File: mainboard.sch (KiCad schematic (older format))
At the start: 32 parts, among them J1 105017-1001, J2 Conn_01x04_Female, J3 Conn_01x02_Female, J4 Conn_01x09_Female, J5 Conn_01x02_Female, J6 Conn_01x02_Female, J7 Conn_01x04_Female, Q1 AOD4184A, U1 ESP32-WROOM-32E_(16MB), U3 AMS1117-3.3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

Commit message: MAND
elco
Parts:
- removed C3: 22u, Capacitor_SMD:C_0805_2012Metric_Pad1.18x1.45mm_HandSolder, symbol Device:C
- removed C8: 470u, Capacitor_SMD:C_0805_2012Metric_Pad1.18x1.45mm_HandSolder, symbol Device:C
- added C3: 470u, Capacitor_SMD:CP_Elec_6.3x5.4, symbol Device:CP
- added C8: 22u, Capacitor_SMD:CP_Elec_6.3x5.4, symbol Device:CP
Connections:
- net 3V3: now also C8.1
- net 5V: now also C3.1
- net GND: now also C3.2, C8.2
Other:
- note added: "Hoofdmodule ESP32\n\n"
- note removed: "Hoofdmodule ESP32\n="
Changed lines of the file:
@@
-$EndComp
-$Comp
-L Device:C C8
-U 1 1 60524F4F
-P 4950 6450
-F 0 "C8" H 5065 6496 50  0000 L CNN
-F 1 "470u" H 5065 6405 50  0000 L CNN
-F 2 "Capacitor_SMD:C_0805_2012Metric_Pad1.18x1.45mm_HandSolder" H 4988 6300 50  0001 C CNN
-F 3 "~" H 4950 6450 50  0001 C CNN
-	1    4950 6450
-	1    0    0    -1
 $EndComp
 $Comp
@@
 SDA
 Text Notes 2250 1300 0    150  ~ 0
-Hoofdmodule ESP32\n=
+Hoofdmodule ESP32\n\n
 Text GLabel 3950 3150 2    50   Input ~ 0
 SDA
@@
 	0    -1   -1   0
 $EndComp
-$Comp
-L Device:C C3
-U 1 1 604CF650
-P 9750 1550
-F 0 "C3" H 9865 1596 50  0000 L CNN
-F 1 "22u" H 9865 1505 50  0000 L CNN
-F 2 "Capacitor_SMD:C_0805_2012Metric_Pad1.18x1.45mm_HandSolder" H 9788 1400 50  0001 C CNN
-F 3 "~" H 9750 1550 50  0001 C CNN
-	1    9750 1550
-	1    0    0    -1
-$EndComp
 Wire Wire Line
 	9350 1700 9750 1700
-Wire Wire Line
-	9650 1400 9750 1400
-Wire Wire Line
-	9750 1400 9950 1400
-Connection ~ 9750 1400
 Connection ~ 4900 1950
 Wire Wire Line
@@
 	0    -1   -1   0
 $EndComp
+$Comp
+L Device:CP C3
+U 1 1 604FA000
+P 4950 6450
+F 0 "C3" H 5068 6496 50  0000 L CNN
+F 1 "470u" H 5068 6405 50  0000 L CNN
+F 2 "Capacitor_SMD:CP_Elec_6.3x5.4" H 4988 6300 50  0001 C CNN
+F 3 "~" H 4950 6450 50  0001 C CNN
+	1    4950 6450
+	1    0    0    -1
+$EndComp
+$Comp
+L Device:CP C8
+U 1 1 604FE2E0
+P 9750 1550
+F 0 "C8" H 9868 1596 50  0000 L CNN
+F 1 "22u" H 9868 1505 50  0000 L CNN
+F 2 "Capacitor_SMD:CP_Elec_6.3x5.4" H 9788 1400 50  0001 C CNN
+F 3 "~" H 9750 1550 50  0001 C CNN
+	1    9750 1550
+	1    0    0    -1
+$EndComp
+Wire Wire Line
+	9650 1400 9750 1400
+Connection ~ 9750 1400
+Wire Wire Line
+	9750 1400 9950 1400
 $EndSCHEMATC

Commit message: wij waren de ir sensor vergeten, oeps
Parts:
- added J8: Conn_01x03_Female, Connector_PinSocket_2.54mm:PinSocket_1x03_P2.54mm_Vertical, symbol Connector:Conn_01x03_Female
- added SW1: SW_SPST, 434111043826:434111043826, symbol Switch:SW_SPST
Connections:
- wire segments 61 -> 59
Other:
- note added: "IR beam"
- moved on the sheet: J3
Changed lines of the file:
@@
 $EndComp
 Wire Wire Line
-	8200 1100 8450 1100
-Wire Wire Line
-	8450 1100 8450 1400
-Wire Wire Line
-	8450 1400 8800 1400
+	8600 1400 8800 1400
 Wire Wire Line
 	8200 1500 8450 1500
@@
 Text GLabel 8600 1100 2    50   Input ~ 0
 5V
-Wire Wire Line
-	8600 1100 8450 1100
-Connection ~ 8450 1100
 NoConn ~ 3900 6500
 NoConn ~ 3900 6600
@@
 INR
 NoConn ~ 2700 6600
-Text Notes 7765 5645 0    150  ~ 0
+Text Notes 7265 5745 0    150  ~ 0
 Pomp
 $Comp
 L Connector:Conn_01x02_Female J3
 U 1 1 6053B267
-P 7820 6160
-F 0 "J3" H 7712 5835 50  0000 C CNN
-F 1 "Conn_01x02_Female" H 7712 5926 50  0000 C CNN
-F 2 "Connector_PinSocket_2.54mm:PinSocket_1x02_P2.54mm_Vertical" H 7820 6160 50  0001 C CNN
-F 3 "~" H 7820 6160 50  0001 C CNN
-	1    7820 6160
-	-1   0    0    1
-$EndComp
-Text GLabel 8020 6060 2    50   Input ~ 0
+P 7320 6260
+F 0 "J3" H 7212 5935 50  0000 C CNN
+F 1 "Conn_01x02_Female" H 7212 6026 50  0000 C CNN
+F 2 "Connector_PinSocket_2.54mm:PinSocket_1x02_P2.54mm_Vertical" H 7320 6260 50  0001 C CNN
+F 3 "~" H 7320 6260 50  0001 C CNN
+	1    7320 6260
+	-1   0    0    1
+$EndComp
+Text GLabel 7520 6160 2    50   Input ~ 0
 Mosfet_Out-
-Text GLabel 8020 6160 2    50   Input ~ 0
+Text GLabel 7520 6260 2    50   Input ~ 0
 5V
 Text Notes 9775 4600 0    150  ~ 0
@@
 Wire Wire Line
 	9750 1400 9950 1400
+$Comp
+L Switch:SW_SPST SW1
+U 1 1 6050D5A1
+P 8400 1100
+F 0 "SW1" H 8400 1335 50  0000 C CNN
+F 1 "SW_SPST" H 8400 1244 50  0000 C CNN
+F 2 "434111043826:434111043826" H 8400 1100 50  0001 C CNN
+F 3 "~" H 8400 1100 50  0001 C CNN
+	1    8400 1100
+	1    0    0    -1
+$EndComp
+Wire Wire Line
+	8600 1100 8600 1400
+Text Notes 8115 5745 0    150  ~ 0
+IR beam
+$Comp
+L Connector:Conn_01x03_Female J8
+U 1 1 60521D0E
+P 8450 6225
+F 0 "J8" H 8342 5900 50  0000 C CNN
+F 1 "Conn_01x03_Female" H 8342 5991 50  0000 C CNN
+F 2 "Connector_PinSocket_2.54mm:PinSocket_1x03_P2.54mm_Vertical" H 8450 6225 50  0001 C CNN
+F 3 "~" H 8450 6225 50  0001 C CNN
+	1    8450 6225
+	-1   0    0    1
+$EndComp
+Text GLabel 8650 6125 2    50   Input ~ 0
+IRB
+Wire Notes Line
+	8072 5320 8072 6538
+Text GLabel 8650 6325 2    50   Input ~ 0
+3V3
+$Comp
+L power:GND #PWR?
+U 1 1 6055B549
+P 8650 6225
+F 0 "#PWR?" H 8650 5975 50  0001 C CNN
+F 1 "GND" V 8655 6097 50  0000 R CNN
+F 2 "" H 8650 6225 50  0001 C CNN
+F 3 "" H 8650 6225 50  0001 C CNN
+	1    8650 6225
+	0    -1   -1   0
+$EndComp
 $EndSCHEMATC

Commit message: lesupdate
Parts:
- removed SW1: SW_SPST, 434111043826:434111043826, symbol Switch:SW_SPST
- added S3: SWITCH-SPDT-SMD-RIGHT-ANGLE, SWITCH_SPST_SMD_A, symbol SparkFun-Switches:SWITCH-SPDT-SMD-RIGHT-ANGLE
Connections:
- net labels added: TFT_EN
- wire segments 59 -> 61
- no-connect marks 7 -> 8
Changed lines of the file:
@@
 Text GLabel 3950 3050 2    50   Input ~ 0
 TFT_MISO
-Text GLabel 3950 3550 2    50   Input ~ 0
-INR
 NoConn ~ 2700 6600
 Text Notes 7265 5745 0    150  ~ 0
@@
 Text GLabel 10400 6050 3    50   Input ~ 0
 TFT_MISO
-Text GLabel 10600 6050 3    50   Input ~ 0
-3V3
 Text GLabel 10500 6050 3    50   Input ~ 0
 TFT_CLK
@@
 Wire Wire Line
 	9750 1400 9950 1400
-$Comp
-L Switch:SW_SPST SW1
-U 1 1 6050D5A1
-P 8400 1100
-F 0 "SW1" H 8400 1335 50  0000 C CNN
-F 1 "SW_SPST" H 8400 1244 50  0000 C CNN
-F 2 "434111043826:434111043826" H 8400 1100 50  0001 C CNN
-F 3 "~" H 8400 1100 50  0001 C CNN
-	1    8400 1100
-	1    0    0    -1
-$EndComp
-Wire Wire Line
-	8600 1100 8600 1400
+Wire Wire Line
+	8600 1100 8600 1200
 Text Notes 8115 5745 0    150  ~ 0
 IR beam
@@
 3V3
 $Comp
-L power:GND #PWR?
+L power:GND #PWR0103
 U 1 1 6055B549
 P 8650 6225
-F 0 "#PWR?" H 8650 5975 50  0001 C CNN
+F 0 "#PWR0103" H 8650 5975 50  0001 C CNN
 F 1 "GND" V 8655 6097 50  0000 R CNN
 F 2 "" H 8650 6225 50  0001 C CNN
@@
 	0    -1   -1   0
 $EndComp
+$Comp
+L SparkFun-Switches:SWITCH-SPDT-SMD-RIGHT-ANGLE S3
+U 1 1 6053016E
+P 8300 1100
+F 0 "S3" H 8350 1476 45  0000 C CNN
+F 1 "SWITCH-SPDT-SMD-RIGHT-ANGLE" H 8350 1392 45  0000 C CNN
+F 2 "SWITCH_SPST_SMD_A" H 8300 1350 20  0001 C CNN
+F 3 "" H 8300 1100 50  0001 C CNN
+F 4 "SWCH-10651" H 8350 1297 60  0000 C CNN "Field4"
+	1    8300 1100
+	1    0    0    -1
+$EndComp
+Wire Wire Line
+	8500 1200 8600 1200
+Connection ~ 8600 1200
+Wire Wire Line
+	8600 1200 8600 1400
+NoConn ~ 8500 1000
+Text GLabel 3950 2850 2    50   Input ~ 0
+TFT_EN
+Text GLabel 10600 6050 3    50   Input ~ 0
+TFT_EN
+Text GLabel 3950 3550 2    50   Input ~ 0
+INR
 $EndSCHEMATC

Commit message: BIEPBOEP
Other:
- note removed: "Moet IO5 aan pullup?"
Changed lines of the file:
@@
 Wire Notes Line
 	470  5320 11210 5320
-Text Notes 5750 2250 0    50   ~ 0
-Moet IO5 aan pullup?
 Wire Notes Line
 	9170 2360 9170 6535

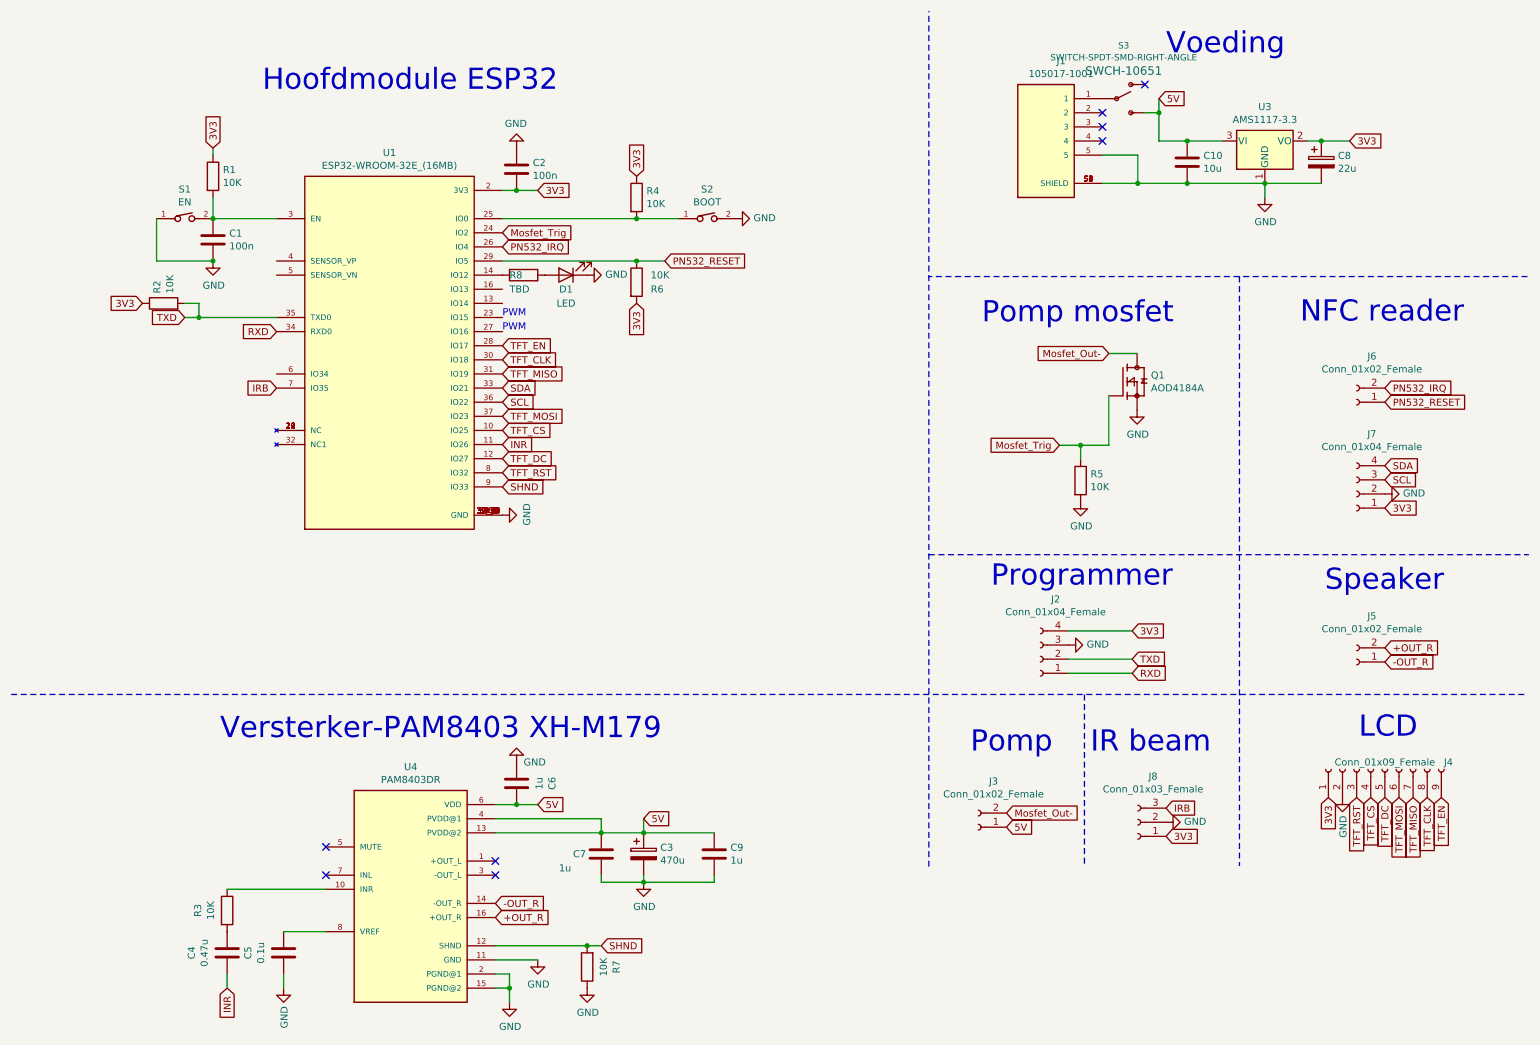
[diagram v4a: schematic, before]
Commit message: checken
update footprints caps
dubbele C8 verwijderd
nfc foute footprint opgelost
checken van alle esp en versterkerpinnen
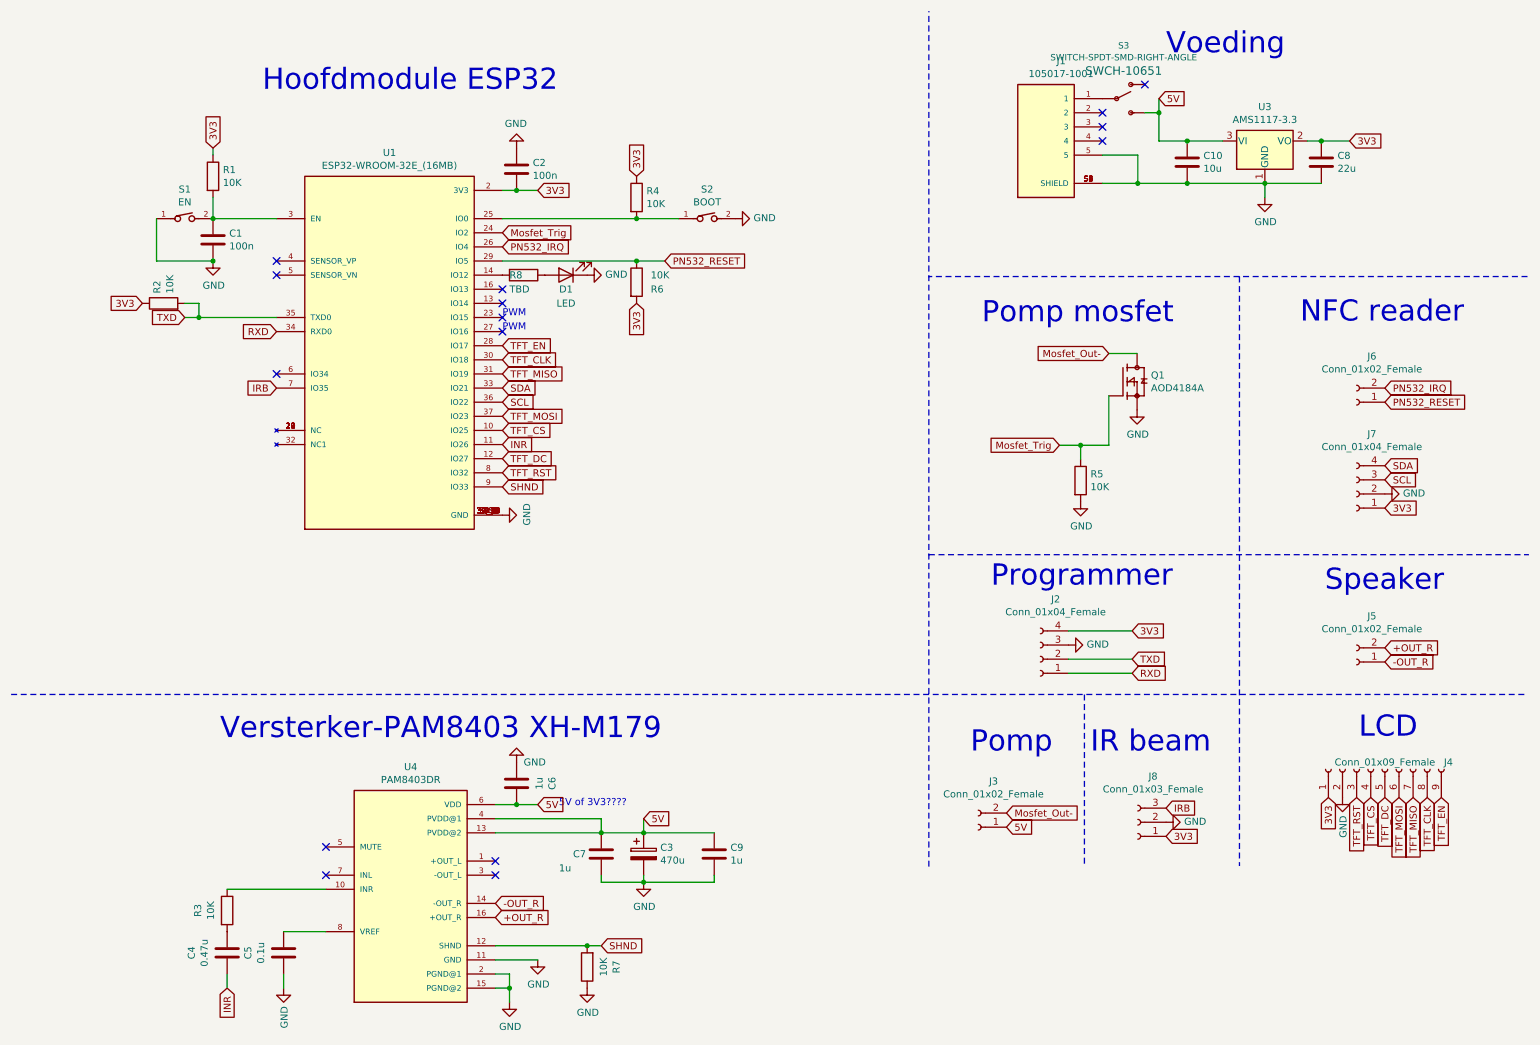
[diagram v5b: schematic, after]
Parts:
- removed C8: 22u, Capacitor_SMD:CP_Elec_6.3x5.4, symbol Device:CP
- added C8: 22u, mylibs:CAPPC3528X210N, symbol Device:C
- C3: footprint Capacitor_SMD:CP_Elec_6.3x5.4 -> Capacitor_THT:CP_Radial_D10.0mm_P5.00mm
- J7: footprint Connector_PinSocket_2.54mm:PinSocket_1x02_P2.54mm_Vertical -> Connector_PinSocket_2.54mm:PinSocket_1x04_P2.54mm_Vertical
- S3: footprint SWITCH_SPST_SMD_A -> Switches:SWITCH_SPST_SMD_A
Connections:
- net 3V3: now also C8.1
- net GND: now also C8.2
- no-connect marks 8 -> 15
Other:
- note added: "5V of 3V3????\n\n"
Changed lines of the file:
@@
 F 0 "J7" H 9892 3475 50  0000 C CNN
 F 1 "Conn_01x04_Female" H 9892 3566 50  0000 C CNN
-F 2 "Connector_PinSocket_2.54mm:PinSocket_1x02_P2.54mm_Vertical" H 10000 3900 50  0001 C CNN
+F 2 "Connector_PinSocket_2.54mm:PinSocket_1x04_P2.54mm_Vertical" H 10000 3900 50  0001 C CNN
 F 3 "~" H 10000 3900 50  0001 C CNN
 	1    10000 3900
@@
 F 0 "C3" H 5068 6496 50  0000 L CNN
 F 1 "470u" H 5068 6405 50  0000 L CNN
-F 2 "Capacitor_SMD:CP_Elec_6.3x5.4" H 4988 6300 50  0001 C CNN
+F 2 "Capacitor_THT:CP_Radial_D10.0mm_P5.00mm" H 4988 6300 50  0001 C CNN
 F 3 "~" H 4950 6450 50  0001 C CNN
 	1    4950 6450
 	1    0    0    -1
 $EndComp
-$Comp
-L Device:CP C8
-U 1 1 604FE2E0
-P 9750 1550
-F 0 "C8" H 9868 1596 50  0000 L CNN
-F 1 "22u" H 9868 1505 50  0000 L CNN
-F 2 "Capacitor_SMD:CP_Elec_6.3x5.4" H 9788 1400 50  0001 C CNN
-F 3 "~" H 9750 1550 50  0001 C CNN
-	1    9750 1550
-	1    0    0    -1
-$EndComp
-Wire Wire Line
-	9650 1400 9750 1400
-Connection ~ 9750 1400
-Wire Wire Line
-	9750 1400 9950 1400
 Wire Wire Line
 	8600 1100 8600 1200
@@
 F 0 "S3" H 8350 1476 45  0000 C CNN
 F 1 "SWITCH-SPDT-SMD-RIGHT-ANGLE" H 8350 1392 45  0000 C CNN
-F 2 "SWITCH_SPST_SMD_A" H 8300 1350 20  0001 C CNN
+F 2 "Switches:SWITCH_SPST_SMD_A" H 8300 1350 20  0001 C CNN
 F 3 "" H 8300 1100 50  0001 C CNN
 F 4 "SWCH-10651" H 8350 1297 60  0000 C CNN "Field4"
@@
 Text GLabel 3950 3550 2    50   Input ~ 0
 INR
+$Comp
+L Device:C C8
+U 1 1 605638F7
+P 9750 1550
+F 0 "C8" H 9865 1596 50  0000 L CNN
+F 1 "22u" H 9865 1505 50  0000 L CNN
+F 2 "mylibs:CAPPC3528X210N" H 9788 1400 50  0001 C CNN
+F 3 "~" H 9750 1550 50  0001 C CNN
+	1    9750 1550
+	1    0    0    -1
+$EndComp
+Wire Wire Line
+	9650 1400 9750 1400
+Connection ~ 9750 1400
+Wire Wire Line
+	9750 1400 9950 1400
+NoConn ~ 2350 3050
+NoConn ~ 2350 2350
+NoConn ~ 2350 2250
+NoConn ~ 3950 2550
+NoConn ~ 3950 2450
+NoConn ~ 3950 2650
+NoConn ~ 3950 2750
+Text Notes 4350 6200 0    50   ~ 0
+5V of 3V3????\n\n
 $EndSCHEMATC

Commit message: condensator vrij gemaakt en hoekjes gefixt
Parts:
- S3: symbol SparkFun-Switches:SWITCH-SPDT-SMD-RIGHT-ANGLE -> mainboard-rescue:SWITCH-SPDT-SMD-RIGHT-ANGLE-SparkFun-Switches
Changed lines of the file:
@@
 $EndComp
 $Comp
-L SparkFun-Switches:SWITCH-SPDT-SMD-RIGHT-ANGLE S3
+L mainboard-rescue:SWITCH-SPDT-SMD-RIGHT-ANGLE-SparkFun-Switches S3
 U 1 1 6053016E
 P 8300 1100

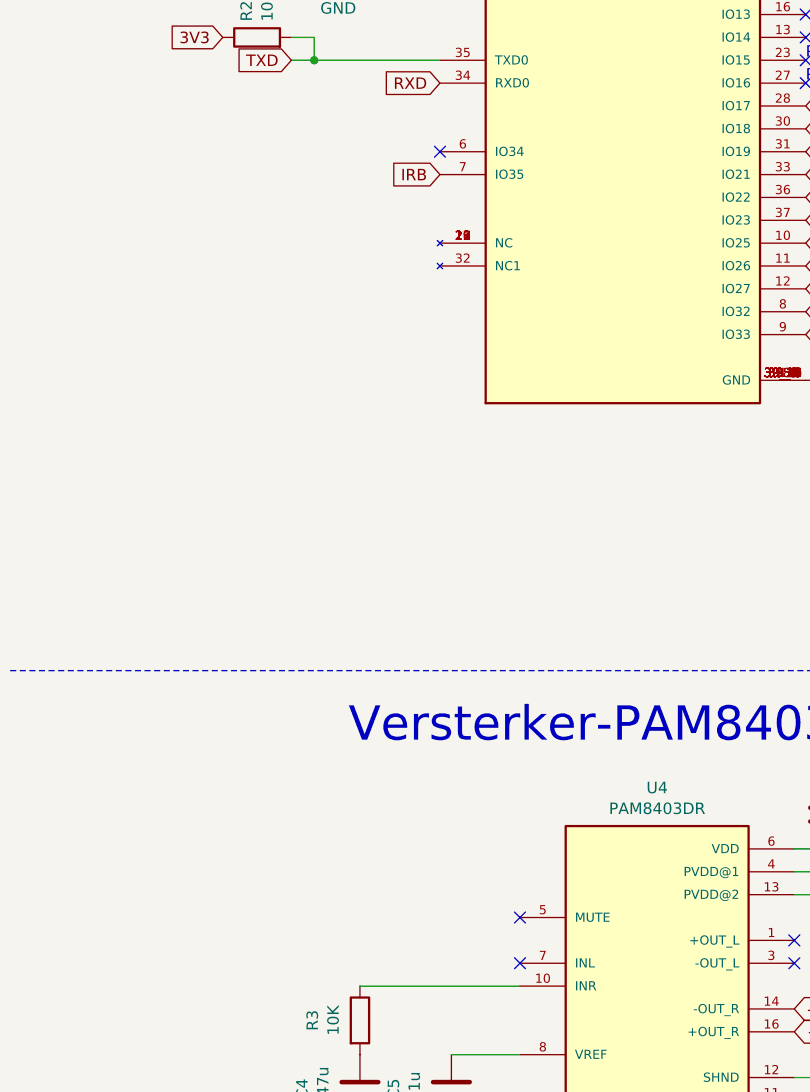
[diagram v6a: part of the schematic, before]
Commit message: fixes
-pullup aan IRB
-mute aan 5V
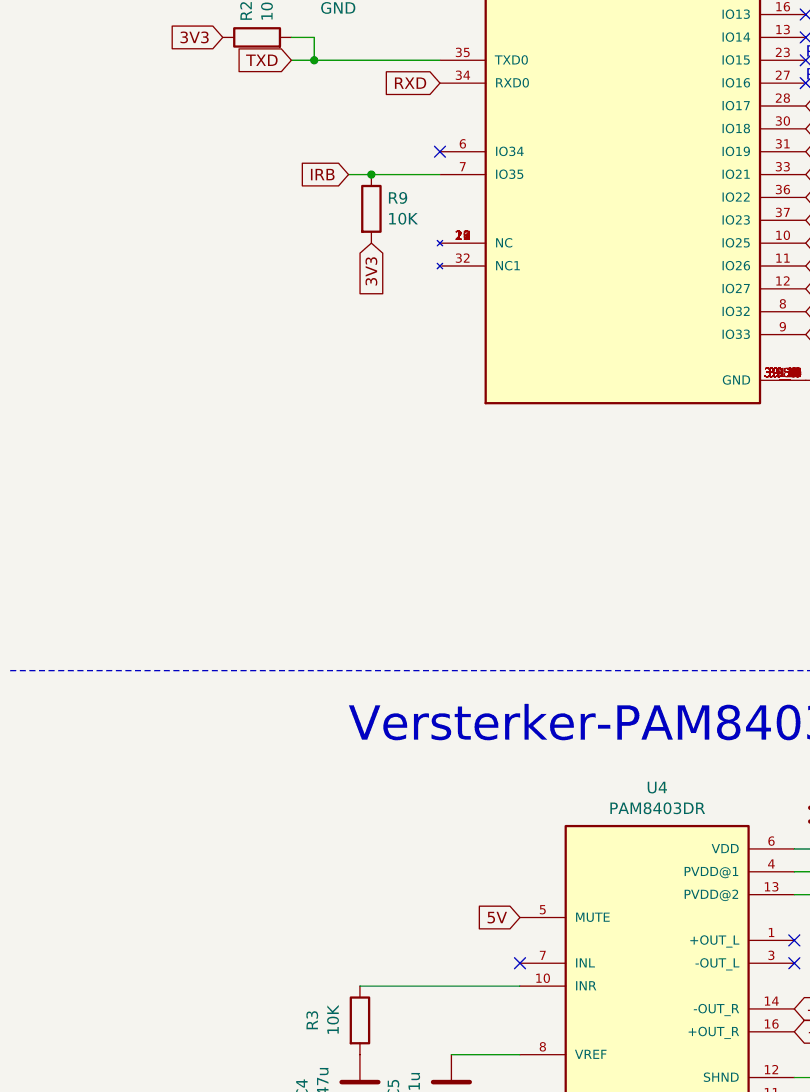
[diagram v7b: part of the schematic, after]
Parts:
- added R9: 10K, Resistor_SMD:R_0805_2012Metric_Pad1.20x1.40mm_HandSolder, symbol Device:R
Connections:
- net 3V3: now also R9.2
- net 5V: now also U4.5 (MUTE)
- net IRB: now also R9.1
- no-connect marks 15 -> 14
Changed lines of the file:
@@
 Text Notes 3950 2750 0    50   ~ 0
 PWM\n
-NoConn ~ 2700 6400
 Text GLabel 3950 3850 2    50   Input ~ 0
 SHND
@@
 Wire Wire Line
 	7895 3555 8045 3555
-Text GLabel 2350 3150 0    50   Input ~ 0
+Text GLabel 1950 3150 0    50   Input ~ 0
 IRB
 Text GLabel 3950 2150 2    50   Input ~ 0
@@
 Text Notes 4350 6200 0    50   ~ 0
 5V of 3V3????\n\n
+$Comp
+L Device:R R9
+U 1 1 606A03C4
+P 2050 3300
+F 0 "R9" H 2120 3346 50  0000 L CNN
+F 1 "10K" H 2120 3255 50  0000 L CNN
+F 2 "Resistor_SMD:R_0805_2012Metric_Pad1.20x1.40mm_HandSolder" V 1980 3300 50  0001 C CNN
+F 3 "~" H 2050 3300 50  0001 C CNN
+	1    2050 3300
+	1    0    0    -1
+$EndComp
+Wire Wire Line
+	1950 3150 2050 3150
+Wire Wire Line
+	2050 3150 2350 3150
+Connection ~ 2050 3150
+Text GLabel 2050 3450 3    50   Input ~ 0
+3V3
+Text GLabel 2700 6400 0    50   Input ~ 0
+5V
 $EndSCHEMATC
